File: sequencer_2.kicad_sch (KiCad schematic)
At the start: 98 parts, among them J1 EuroPower16 THT, Q10 BC338, Q3 BC338, Q4 BC338, Q5 BC338, Q6 BC338, Q7 BC338, Q8 BC338, Q9 BC338, U2 MCP6002-xP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

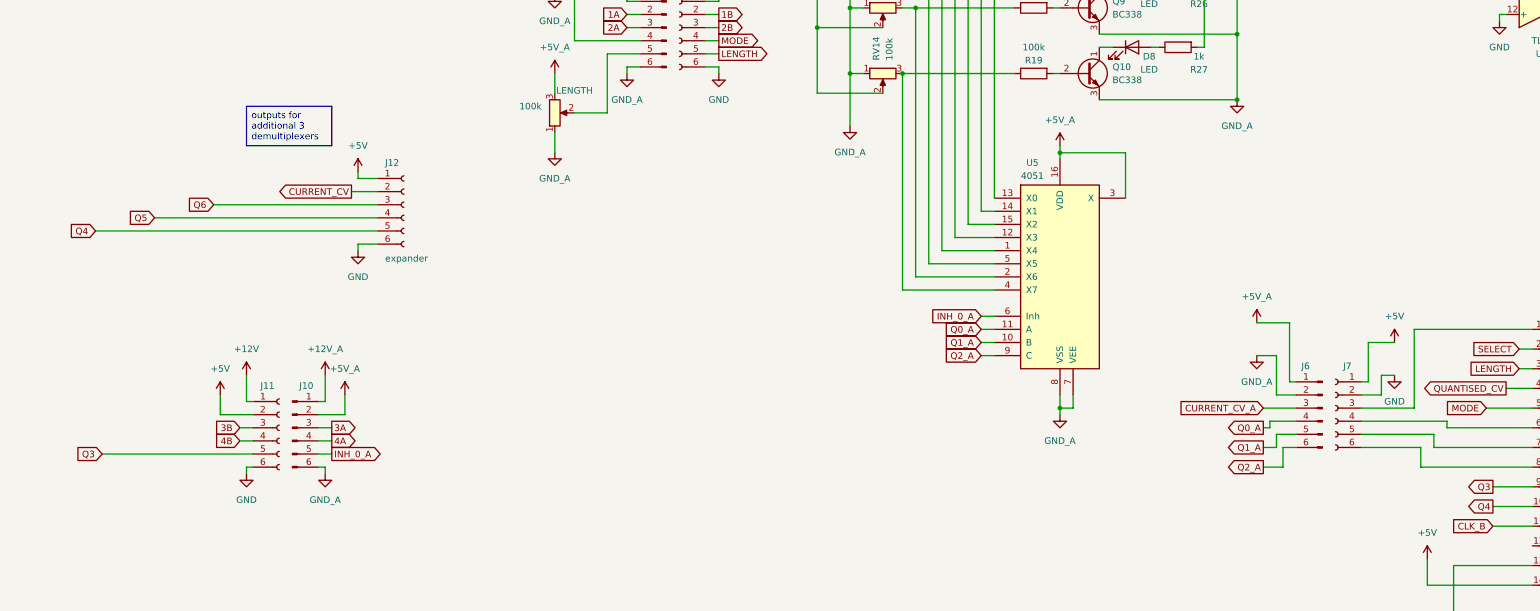
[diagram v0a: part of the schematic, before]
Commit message: J9 and J12 rework.
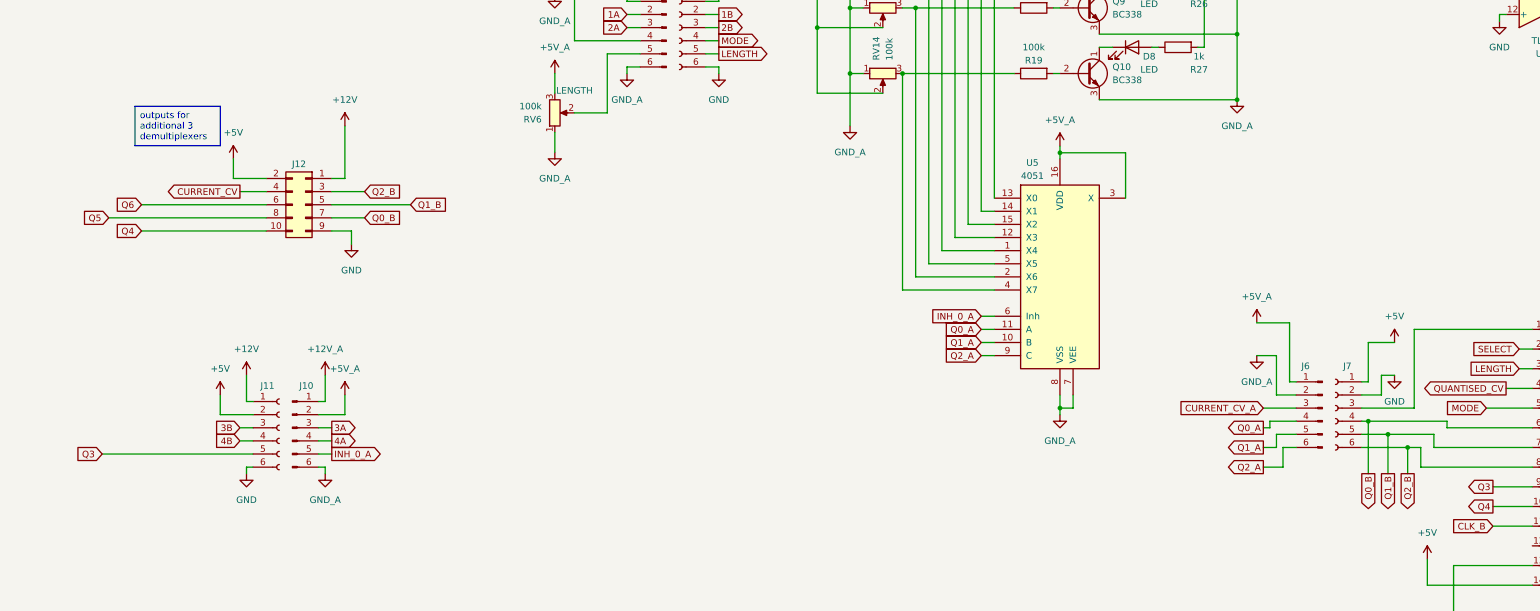
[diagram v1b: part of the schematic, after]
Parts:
- J12: footprint Connector_PinSocket_2.54mm:PinSocket_1x06_P2.54mm_Vertical -> Connector_PinSocket_2.54mm:PinSocket_2x05_P2.54mm_Vertical; symbol Connector:Conn_01x06_Socket -> Connector_Generic:Conn_02x05_Odd_Even
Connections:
- net +12V: now also J12.1 (Pin_1)
- net +5V: now also J12.2 (Pin_2); no longer J12.1 (Pin_1)
- net CURRENT_CV: now also J12.4 (Pin_4); no longer J12.2 (Pin_2)
- net GND: now also J12.9 (Pin_9); no longer J12.6 (Pin_6)
- net Q4: now also J12.10 (Pin_10); no longer J12.5 (Pin_5)
- net Q5: now also J12.8 (Pin_8); no longer J12.4 (Pin_4)
- net Q6: now also J12.6 (Pin_6); no longer J12.3 (Pin_3)
- net Q0_B: now reaches J7.4 (Pin_4), U6.6 (P100_A5_D5_SCL1)
- net Q0_B: now also J12.7 (Pin_7)
- net Q1_B: now reaches J7.5 (Pin_5), U6.7 (P302_D6_SDA2_TXD2)
- net Q1_B: now also J12.5 (Pin_5)
- net Q2_B: now reaches J7.6 (Pin_6), U6.8 (P301_D7_SCL2_RXD2)
- net Q2_B: now also J12.3 (Pin_3)

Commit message: RST input.
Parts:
- added C17: 1n, Capacitor_THT:C_Disc_D3.4mm_W2.1mm_P2.50mm, symbol Device:C
- added J13: ~, EuroRackTools:Jack_3.5mm_QingPu_WQP-PJ398SM_Vertical_CircularHoles, symbol EuroRackTools:Thonkiconn
- added R1, R2: 100k, Resistor_THT:R_Axial_DIN0207_L6.3mm_D2.5mm_P7.62mm_Horizontal, symbol Device:R
- added R3: 47k, Resistor_THT:R_Axial_DIN0207_L6.3mm_D2.5mm_P7.62mm_Horizontal, symbol Device:R
- added RV17, RV18: 100k, Potentiometer_THT:Potentiometer_Bourns_3296W_Vertical, symbol Device:R_Potentiometer_Trim
- J8: footprint Connector_PinHeader_2.54mm:PinHeader_1x06_P2.54mm_Vertical -> Connector_PinHeader_2.54mm:PinHeader_1x07_P2.54mm_Vertical; symbol Connector:Conn_01x06_Pin -> Connector:Conn_01x07_Pin
- J9: footprint Connector_PinSocket_2.54mm:PinSocket_1x06_P2.54mm_Vertical -> Connector_PinSocket_2.54mm:PinSocket_1x07_P2.54mm_Vertical; symbol Connector:Conn_01x06_Socket -> Connector:Conn_01x07_Pin
- U2: value MCP6002-xP -> MCP6004-xP; footprint Package_DIP:DIP-8_W7.62mm_LongPads -> Package_DIP:DIP-14_W7.62mm_LongPads; symbol Amplifier_Operational:MCP6002-xP -> Amplifier_Operational:MCP6004
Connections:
- net CLK_B is gone; now on net CLK: U6.11 (P109_D10_MOSI9)
- net SELECT_A is gone; now on net SELECT: C6.2, RV4.3, U2.7
- net +5V: now also U2.4 (V+); no longer U2.8 (V+)
- net 3A: now also J8.4 (Pin_4), J13.T
- net 3B: now also J9.4 (Pin_4), R2.1
- net A_REF_-10V: now also RV17.3
- net GND: now also J9.7 (Pin_7), U2.10 (+), U2.11 (V-), RV17.1; no longer J9.6 (Pin_6), U2.4 (V-)
- net GND_A: now also J8.7 (Pin_7), J13.S; no longer J8.6 (Pin_6)
- net LENGTH: now also J9.6 (Pin_6); no longer J9.5 (Pin_5)
- net MODE: now also J9.5 (Pin_5); no longer J9.4 (Pin_4)
- net at RV6.2: now also J8.6 (Pin_6); no longer J8.5 (Pin_5)
- net RST: now reaches U6.19 (P101_D15_MOSI0)
- net RST: now also U2.8, C17.2, RV18.3
- net at RV5.2: now also J8.5 (Pin_5); no longer J8.4 (Pin_4)
- net CLK_A renamed CLK
- new net: C17.1, R1.2, R2.2, R3.1, U2.9 (-)
- new net: R1.1, RV17.2
- new net: R3.2, RV18.1, RV18.2
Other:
- moved on the sheet: J10, J11, J12, RV5, RV6
